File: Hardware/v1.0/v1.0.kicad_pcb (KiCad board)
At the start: 2 copper layers, 58.9 x 39.8 mm, 23 parts, among them J1 Barrel_Jack_Switch, J2 Conn_01x03_Male, K1 G5LE-1, Q2 BC237, U1 LM358, U2 LM555

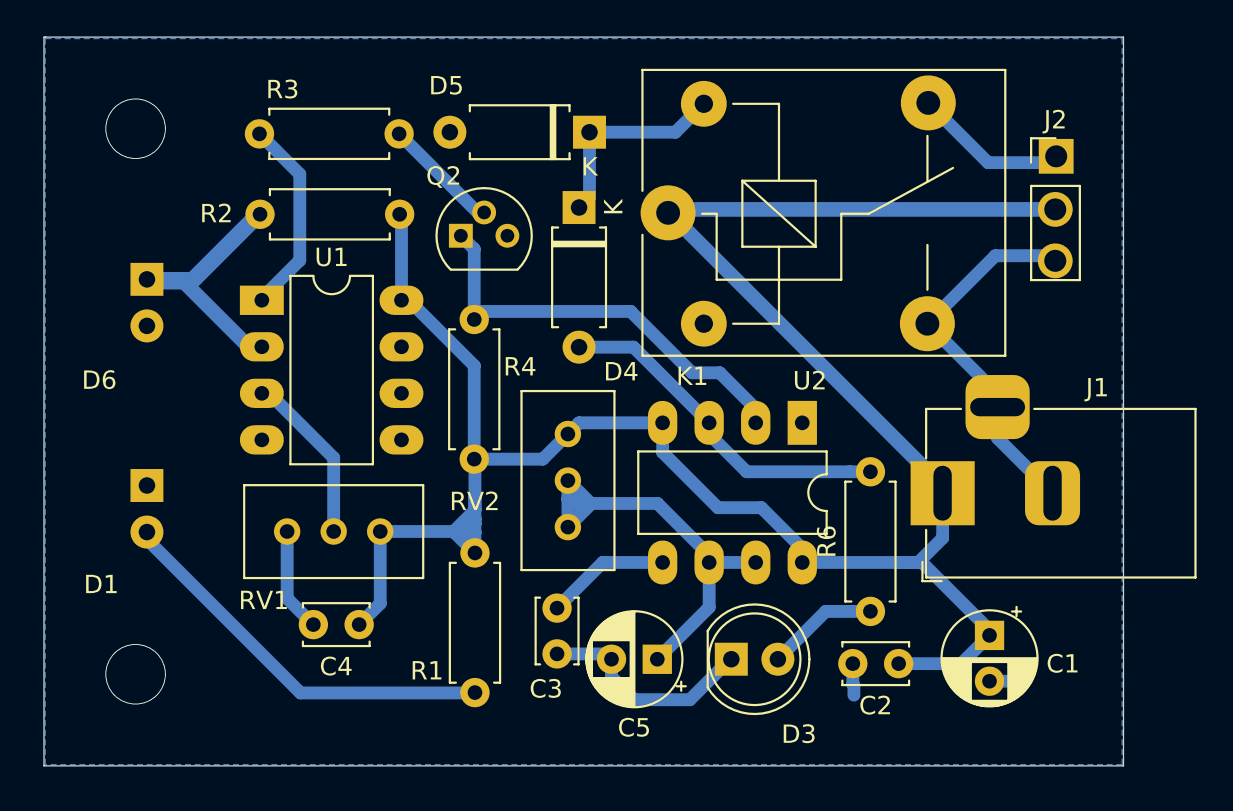
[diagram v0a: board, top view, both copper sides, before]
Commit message: design with MOSFET
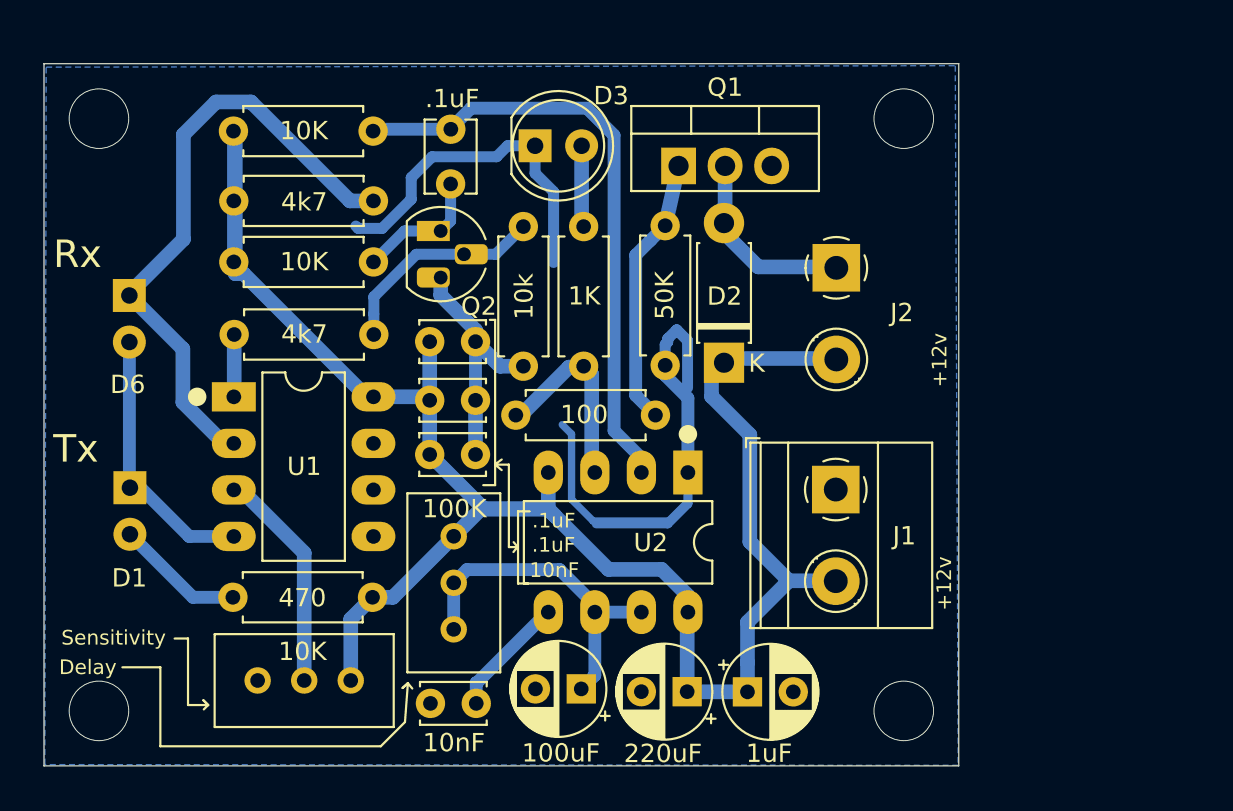
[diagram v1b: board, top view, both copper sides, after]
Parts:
- removed D4, D5: 1N4004, Diode_THT:D_A-405_P7.62mm_Horizontal
- removed K1: G5LE-1, Relay_THT:Relay_SPDT_SANYOU_SRD_Series_Form_C
- added C6: .1uF, Capacitor_THT:C_Disc_D3.8mm_W2.6mm_P2.50mm, F.Cu at (106.4, 119.5)
- added C7: 1uF, Capacitor_THT:CP_Radial_D5.0mm_P2.50mm, F.Cu at (122.6, 149.9)
- added C8: .1uF, Capacitor_THT:C_Disc_D3.4mm_W2.1mm_P2.50mm, F.Cu at (105.3, 134.0)
- added D2: 1N4007, Diode_THT:D_DO-41_SOD81_P7.62mm_Horizontal, F.Cu at (121.3, 132.0)
- added Q1: IRF740, Package_TO_SOT_THT:TO-220-3_Vertical, F.Cu at (118.8, 121.2)
- added R5: 10K, Resistor_THT:R_Axial_DIN0207_L6.3mm_D2.5mm_P7.62mm_Horizontal, F.Cu at (102.2, 119.3)
- added R7: 10k, Resistor_THT:R_Axial_DIN0207_L6.3mm_D2.5mm_P7.62mm_Horizontal, F.Cu at (110.4, 124.5)
- added R8: 100, Resistor_THT:R_Axial_DIN0207_L6.3mm_D2.5mm_P7.62mm_Horizontal, F.Cu at (110.0, 134.8)
- added R9: 50K, Resistor_THT:R_Axial_DIN0207_L6.3mm_D2.5mm_P7.62mm_Horizontal, F.Cu at (118.1, 124.5)
- C1: value 100uF/25V -> 220uF
- C2: value 100n -> .1uF
- C3, C4: value 100n -> 10nF
- C5: value 100uF/25V -> 100uF
- J1: value Barrel_Jack_Switch -> input; footprint Connector_BarrelJack:BarrelJack_Horizontal -> TerminalBlock_Phoenix:TerminalBlock_Phoenix_MKDS-1,5-2_1x02_P5.00mm_Horizontal
- J2: value Conn_01x03_Male -> relay conn; footprint Connector_PinHeader_2.54mm:PinHeader_1x03_P2.54mm_Vertical -> TerminalBlock_Phoenix:TerminalBlock_Phoenix_MKDS-1,5-2_1x02_P5.00mm_Horizontal
- Q2: footprint Package_TO_SOT_THT:TO-92 -> Package_TO_SOT_THT:TO-92_HandSolder
- RV1: value R_POT_Small -> 10K
- moved C2 31.0 mm to (105.3, 130.8), turned to 0 degrees
- moved D3 30.0 mm to (111.0, 120.1)
- moved R6 26.2 mm to (113.7, 124.5), turned to 270 degrees
- moved C1 16.8 mm to (119.3, 149.9), turned to 180 degrees
- moved J2 13.3 mm to (127.5, 126.8), turned to 270 degrees
- moved R3 11.0 mm to (94.6, 130.4)
- moved C4 10.0 mm to (105.3, 137.0), turned to 0 degrees
- moved RV2 8.36 mm to (106.6, 141.4)
- moved RV1 8.29 mm to (101.0, 149.3)
- moved C3 6.82 mm to (107.8, 150.6), turned to 180 degrees
- moved U2 6.80 mm to (119.4, 138.0)
- moved R4 6.33 mm to (102.2, 126.5), turned to 180 degrees
- moved R2 6.23 mm to (102.2, 123.1), turned to 180 degrees
- moved R1 6.09 mm to (102.2, 144.8), turned to 180 degrees
- moved J1 5.83 mm to (127.4, 138.9), turned to 270 degrees
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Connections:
- J1 pad 1: +12V -> GND
- J1 pad 2: GND -> +12V
- J2 pad 1: /NC -> Net-(D2-Pad2)
- Q2 pad 1: Net-(Q2-Pad1) -> Net-(C6-Pad2)
- R4 pad 1: Net-(Q2-Pad1) -> Net-(C6-Pad2)
- U2 pad 2: Net-(Q2-Pad1) -> Net-(C6-Pad1)
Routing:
- net +12V: track 146.5 -> 108.5 mm
- net GND: track 41.9 -> 79.8 mm
- net Net-(C6-Pad1): track 0.00 -> 33.4 mm
- net Net-(Q2-Pad1): track 23.4 -> 0.00 mm
- net Net-(Q1-Pad1): track 0.00 -> 14.8 mm
- net Net-(D1-Pad2): track 21.8 -> 7.04 mm
- net Net-(D4-Pad1): track 11.2 -> 0.00 mm
- net Net-(D2-Pad2): track 0.00 -> 10.6 mm
- net /NC: track 8.29 -> 0.00 mm
- net Net-(R6-Pad2): track 19.1 -> 10.9 mm
- net Net-(R3-Pad1): track 10.8 -> 3.41 mm
- net Net-(C6-Pad2): track 0.00 -> 7.16 mm
- net Net-(C5-Pad1): track 24.6 -> 18.8 mm
- net Net-(Q2-Pad2): track 6.42 -> 11.8 mm
- net Net-(D6-Pad1): track 30.0 -> 34.1 mm
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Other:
- board size 58.9 x 39.8 mm -> 49.9 x 38.3 mm
- board text added: "+12v"
- board text added: "--Infiniti Systems--"
- board text added: "Delay"
- board text added: "Devaji"
- board text added: "Dispenser"
- board text added: "Rx"
- board text added: "Sensitivity"
- board text added: "Tx"
- board text added: "v2.0"

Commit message: new gerber
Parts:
- moved C7 2.10 mm to (124.7, 149.9)
- moved C1 1.08 mm to (120.4, 149.9)
- moved C5 0.51 mm to (114.0, 149.9)
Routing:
- net +12V: track 108.5 -> 109.6 mm
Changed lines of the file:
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@@
   )
   (setup
-    (last_trace_width 0.25)
+    (last_trace_width 0.8)
     (user_trace_width 0.3)
     (user_trace_width 0.35)
@@
     (visible_elements 7FFFFFFF)
     (pcbplotparams
-      (layerselection 0x00000_fffffffe)
+      (layerselection 0x010fc_ffffffff)
       (usegerberextensions false)
       (usegerberattributes false)
@@
       (padsonsilk false)
       (subtractmaskfromsilk false)
-      (outputformat 4)
+      (outputformat 1)
       (mirror false)
-      (drillshape 2)
+      (drillshape 0)
       (scaleselection 1)
-      (outputdirectory "PDF/"))
+      (outputdirectory "Gerber/"))
   )
   (net 0 "")
@@
   )
   (module Capacitor_THT:CP_Radial_D5.0mm_P2.50mm (layer F.Cu)
-    (at 122.61 149.93)
+    (at 124.714 149.93)
     (descr "CP, Radial series, Radial, pin pitch=2.50mm, , diameter=5mm, Electrolytic Capacitor")
     (tags "CP Radial series Radial pin pitch 2.50mm  diameter 5mm Electrolytic Capacitor")
@@
   )
   (module Capacitor_THT:CP_Radial_D5.0mm_P2.50mm (layer F.Cu)
-    (at 119.32 149.92 180)
+    (at 120.396 149.92 180)
     (descr "CP, Radial series, Radial, pin pitch=2.50mm, , diameter=5mm, Electrolytic Capacitor")
     (tags "CP Radial series Radial pin pitch 2.50mm  diameter 5mm Electrolytic Capacitor")
@@
   )
   (module Capacitor_THT:CP_Radial_D5.0mm_P2.50mm (layer F.Cu)
-    (at 113.54 149.77 180)
+    (at 114.046 149.86 180)
     (descr "CP, Radial series, Radial, pin pitch=2.50mm, , diameter=5mm, Electrolytic Capacitor")
     (tags "CP Radial series Radial pin pitch 2.50mm  diameter 5mm Electrolytic Capacitor")
@@
   (segment (start 113.01 139.43) (end 113.01 135.86) (width 0.4) (layer B.Cu) (net 1))
   (segment (start 113.01 135.86) (end 112.5 135.35) (width 0.4) (layer B.Cu) (net 1))
-  (segment (start 122.61 148.33) (end 122.61 149.93) (width 0.8) (layer B.Cu) (net 2))
-  (segment (start 122.61 146.131523) (end 122.61 148.33) (width 0.8) (layer B.Cu) (net 2))
-  (segment (start 124.871523 143.87) (end 122.61 146.131523) (width 0.8) (layer B.Cu) (net 2))
-  (segment (start 126.71 143.87) (end 124.871523 143.87) (width 0.8) (layer B.Cu) (net 2))
-  (segment (start 119.33 149.93) (end 119.32 149.92) (width 0.8) (layer B.Cu) (net 2))
-  (segment (start 122.61 149.93) (end 119.33 149.93) (width 0.8) (layer B.Cu) (net 2))
-  (segment (start 119.32 145.62) (end 119.36 145.58) (width 0.8) (layer B.Cu) (net 2))
-  (segment (start 119.32 149.92) (end 119.32 145.62) (width 0.8) (layer B.Cu) (net 2))
   (segment (start 111.74 137.96) (end 111.74 139.96) (width 0.8) (layer B.Cu) (net 2))
   (segment (start 100.96 145.96) (end 102.15 144.77) (width 0.8) (layer B.Cu) (net 2))
@@
   (segment (start 108.24 139.95) (end 111.73 139.95) (width 0.8) (layer B.Cu) (net 2))
   (segment (start 105.27 136.98) (end 108.24 139.95) (width 0.8) (layer B.Cu) (net 2))
-  (segment (start 120.71 131.74) (end 120.65 131.8) (width 0.8) (layer B.Cu) (net 2))
-  (segment (start 126.9 131.74) (end 120.71 131.74) (width 0.8) (layer B.Cu) (net 2))
-  (segment (start 122.74 141.738477) (end 124.871523 143.87) (width 0.8) (layer B.Cu) (net 2))
-  (segment (start 122.74 135.9) (end 122.74 141.738477) (width 0.8) (layer B.Cu) (net 2))
-  (segment (start 120.65 131.8) (end 120.65 133.81) (width 0.8) (layer B.Cu) (net 2))
-  (segment (start 120.65 133.81) (end 122.74 135.9) (width 0.8) (layer B.Cu) (net 2))
   (segment (start 119.36 144.68) (end 119.36 145.58) (width 0.8) (layer B.Cu) (net 2))
   (segment (start 117.93 143.25) (end 119.36 144.68) (width 0.8) (layer B.Cu) (net 2))
@@
   (segment (start 94.56 119.33) (end 94.66 119.43) (width 0.8) (layer B.Cu) (net 2))
   (segment (start 94.66 119.43) (end 94.66 127.11) (width 0.8) (layer B.Cu) (net 2))
+  (segment (start 119.32 145.62) (end 119.36 145.58) (width 0.8) (layer B.Cu) (net 2))
+  (segment (start 126.366 143.89) (end 127.43 143.89) (width 0.8) (layer B.Cu) (net 2))
+  (segment (start 124.714 149.93) (end 124.714 145.542) (width 0.8) (layer B.Cu) (net 2))
+  (segment (start 124.714 145.542) (end 126.366 143.89) (width 0.8) (layer B.Cu) (net 2))
+  (segment (start 121.56 131.74) (end 126.9 131.74) (width 0.8) (layer B.Cu) (net 2))
+  (segment (start 121.33 131.97) (end 121.56 131.74) (width 0.8) (layer B.Cu) (net 2))
+  (segment (start 121.33 134.03) (end 121.33 131.97) (width 0.8) (layer B.Cu) (net 2))
+  (segment (start 123.19 135.89) (end 121.33 134.03) (width 0.8) (layer B.Cu) (net 2))
+  (segment (start 123.19 140.716) (end 123.19 135.89) (width 0.8) (layer B.Cu) (net 2))
+  (segment (start 127.43 143.89) (end 126.364 143.89) (width 0.8) (layer B.Cu) (net 2))
+  (segment (start 126.364 143.89) (end 123.19 140.716) (width 0.8) (layer B.Cu) (net 2))
+  (segment (start 120.406 149.93) (end 120.396 149.92) (width 0.8) (layer B.Cu) (net 2))
+  (segment (start 124.714 149.93) (end 120.406 149.93) (width 0.8) (layer B.Cu) (net 2))
+  (segment (start 120.396 146.616) (end 119.36 145.58) (width 0.8) (layer B.Cu) (net 2))
+  (segment (start 120.396 149.92) (end 120.396 146.616) (width 0.8) (layer B.Cu) (net 2))
   (segment (start 107.81 149.42863) (end 107.81 150.56) (width 0.7) (layer B.Cu) (net 3))
   (segment (start 107.85137 149.42863) (end 107.81 149.42863) (width 0.7) (layer B.Cu) (net 3))
@@
   (segment (start 111.7 145.58) (end 107.85137 149.42863) (width 0.7) (layer B.Cu) (net 3))
   (segment (start 116.82 145.58) (end 114.28 145.58) (width 0.7) (layer B.Cu) (net 4))
-  (segment (start 114.28 149.03) (end 113.54 149.77) (width 0.7) (layer B.Cu) (net 4))
-  (segment (start 114.28 145.58) (end 114.28 149.03) (width 0.7) (layer B.Cu) (net 4))
   (segment (start 107.299999 143.260001) (end 106.58 143.98) (width 0.7) (layer B.Cu) (net 4))
   (segment (start 112.360001 143.260001) (end 107.299999 143.260001) (width 0.7) (layer B.Cu) (net 4))
@@
   (segment (start 114.28 145.18) (end 112.360001 143.260001) (width 0.7) (layer B.Cu) (net 4))
   (segment (start 106.58 146.52) (end 106.58 143.98) (width 0.7) (layer B.Cu) (net 4))
+  (segment (start 114.28 145.58) (end 114.046 149.86) (width 0.7) (layer B.Cu) (net 4))
   (segment (start 113.56 124.43) (end 113.67 124.54) (width 0.8) (layer B.Cu) (net 5))
   (segment (start 113.56 120.13) (end 113.56 124.43) (width 0.8) (layer B.Cu) (net 5))
